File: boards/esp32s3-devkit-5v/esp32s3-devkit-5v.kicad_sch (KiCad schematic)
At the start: 62 parts, among them J1 Conn_01x02_Pin, J2 USB_C_Receptacle_USB2.0_16P, J3 Conn_01x02_Pin, J4 Conn_01x04_Pin, Q1 AO3401A, Q2 AO3401A, Q3 MMBT3904, SW1 MK-12C03-G015, SW2 RESET, SW3 BOOT, U1 TPS63070RNMR, U2 TPS63070RNMR, U3 ESP32-S3-WROOM-1-N16, U4 USBLC6-2SC6, U5 RV-3028-C7, U6 MAX98357A

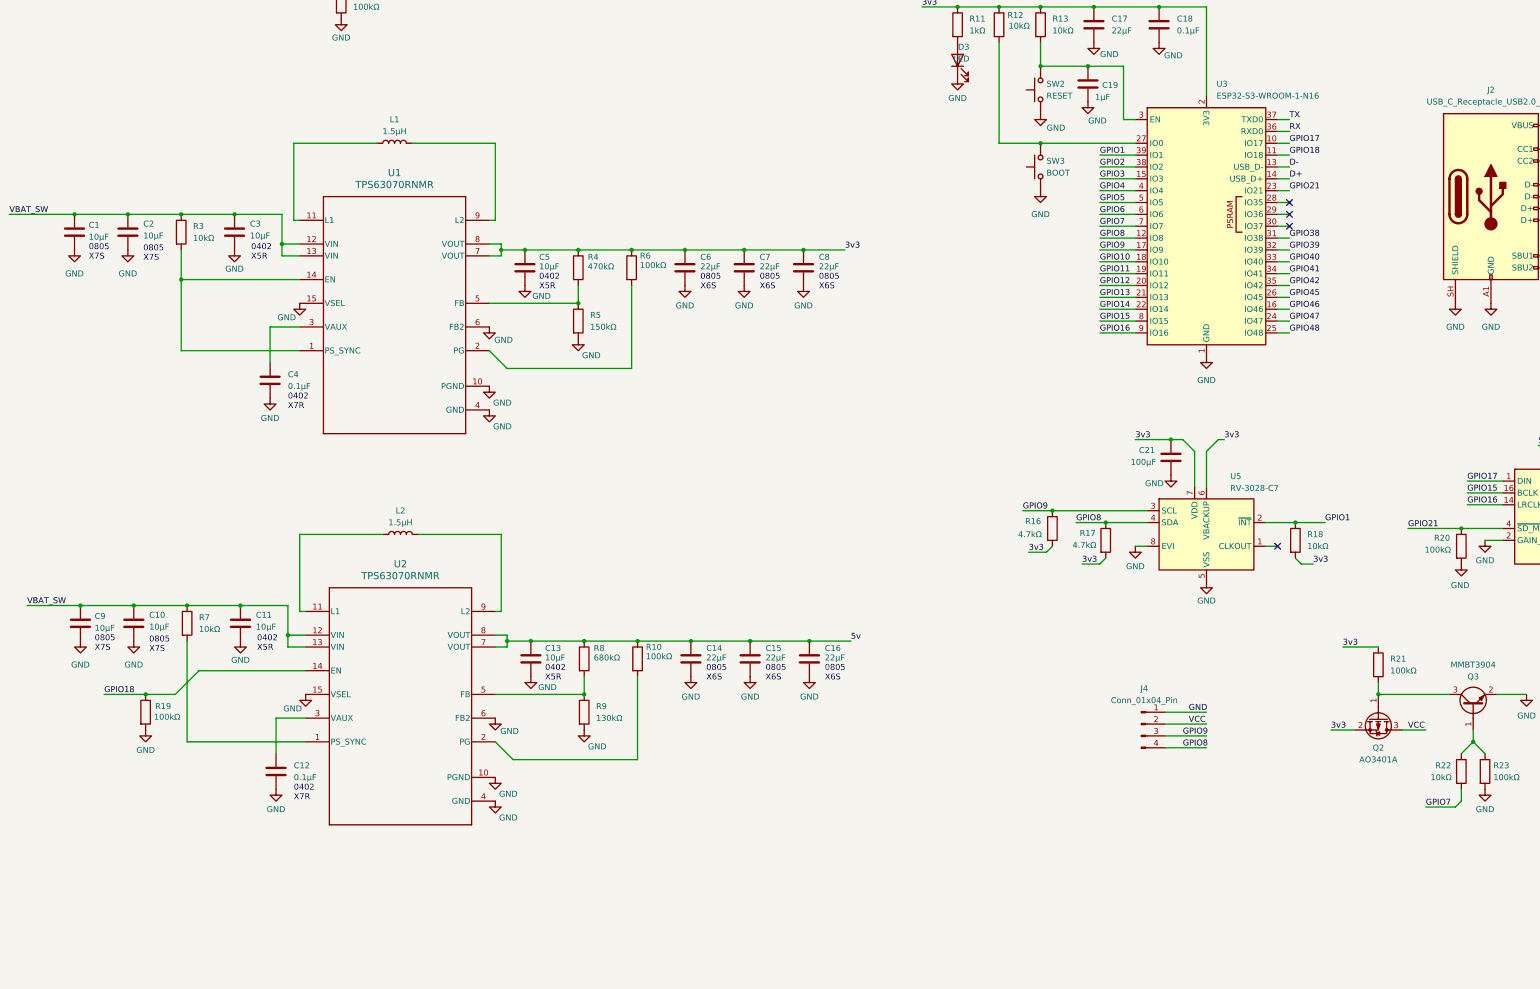
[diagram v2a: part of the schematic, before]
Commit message: feat(esp32s3-devkit-5v): add 4 front-panel buttons
Mode/Vol+/Vol-/4th on GPIO4/5/6/10 (matches cube_browns.ino PIN_MODE/VOL_UP/
VOL_DOWN; GPIO10 is RTC-capable so the 4th can also wake from deep sleep).

Each button: SW_Push (TS-1187A) to the GPIO node + GND, 10k pull-up to 3v3
(robust idle level for EXT1 deep-sleep wake), 100nF debounce to GND. Active-low,
matching the firmware's INPUT_PULLUP.

Added programmatically via kicad-skip, grid-aligned; connectivity by local labels
(this sheet wires everything, incl. GND/3v3, with local labels). ERC adds no new
violations. Positions are functional — hand-tidy the layout as desired.

Co-Authored-By: Claude Opus 4.8 <noreply@anthropic.com>
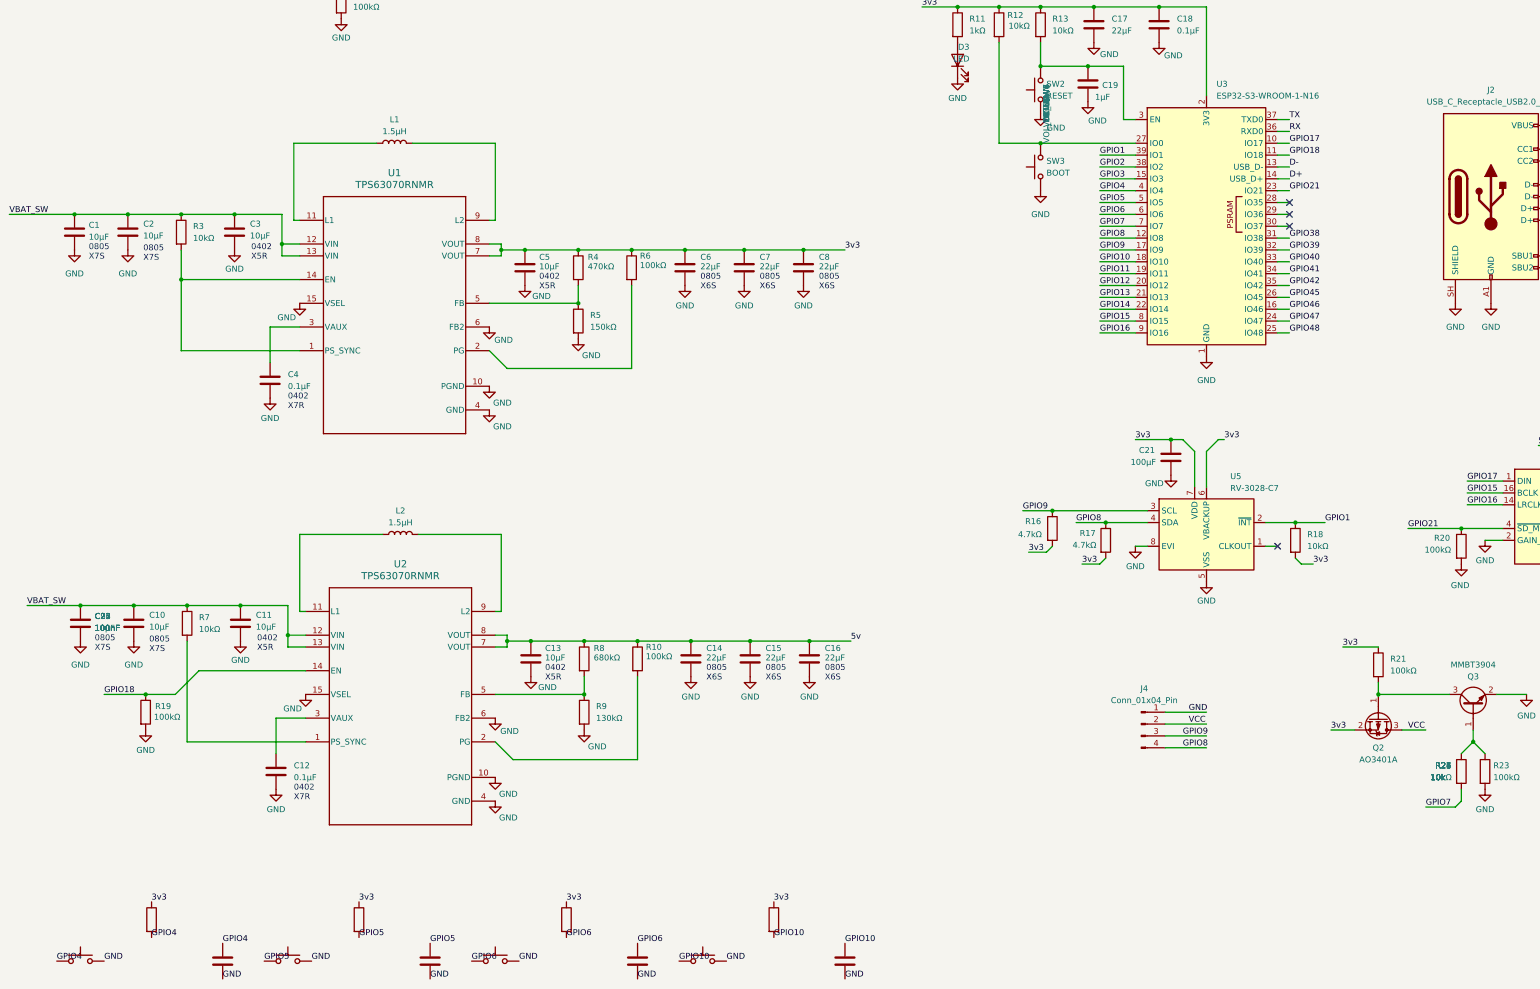
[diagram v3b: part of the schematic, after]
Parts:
- added C22, C23, C24, C25: 100nF, Capacitor_SMD:C_0805_2012Metric, symbol Device:C
- added R24, R25, R26, R27: 10k, symbol Device:R
- added SW4: MODE, Button_Switch_SMD:SW_Push_1P1T_XKB_TS-1187A, symbol Switch:SW_Push
- added SW5: VOL_UP, Button_Switch_SMD:SW_Push_1P1T_XKB_TS-1187A, symbol Switch:SW_Push
- added SW6: VOL_DOWN, Button_Switch_SMD:SW_Push_1P1T_XKB_TS-1187A, symbol Switch:SW_Push
- added SW7: BTN4, Button_Switch_SMD:SW_Push_1P1T_XKB_TS-1187A, symbol Switch:SW_Push
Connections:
- net 3v3: now also R24.1, R25.1, R26.1, R27.1
- net GND: now also C22.2, C23.2, C24.2, C25.2, SW4.2, SW5.2, SW6.2, SW7.2
- net GPIO10: now also C25.1, R27.2, SW7.1
- net GPIO4: now also C22.1, R24.2, SW4.1
- net GPIO5: now also C23.1, R25.2, SW5.1
- net GPIO6: now also C24.1, R26.2, SW6.1
